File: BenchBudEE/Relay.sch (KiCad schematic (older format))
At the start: 0 parts

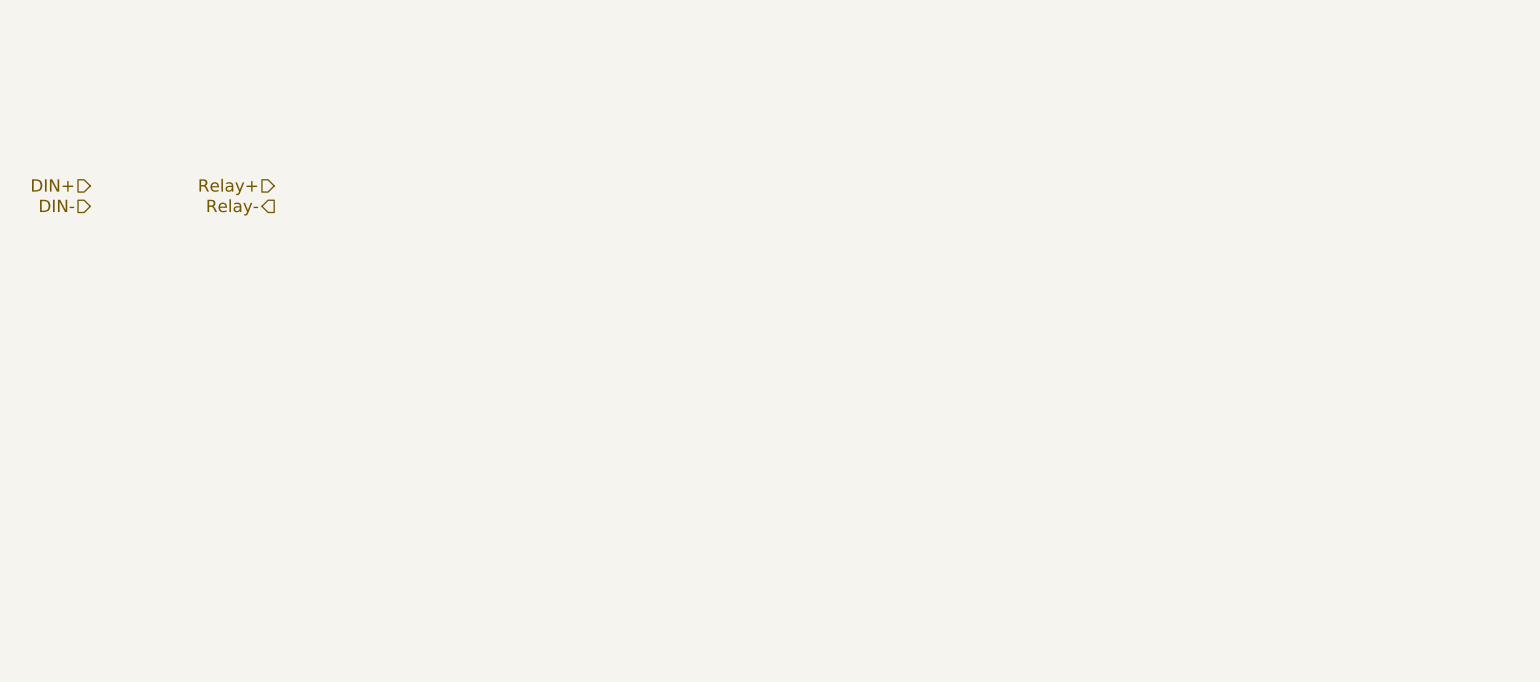
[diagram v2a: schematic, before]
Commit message: Implementing Relay schematic.
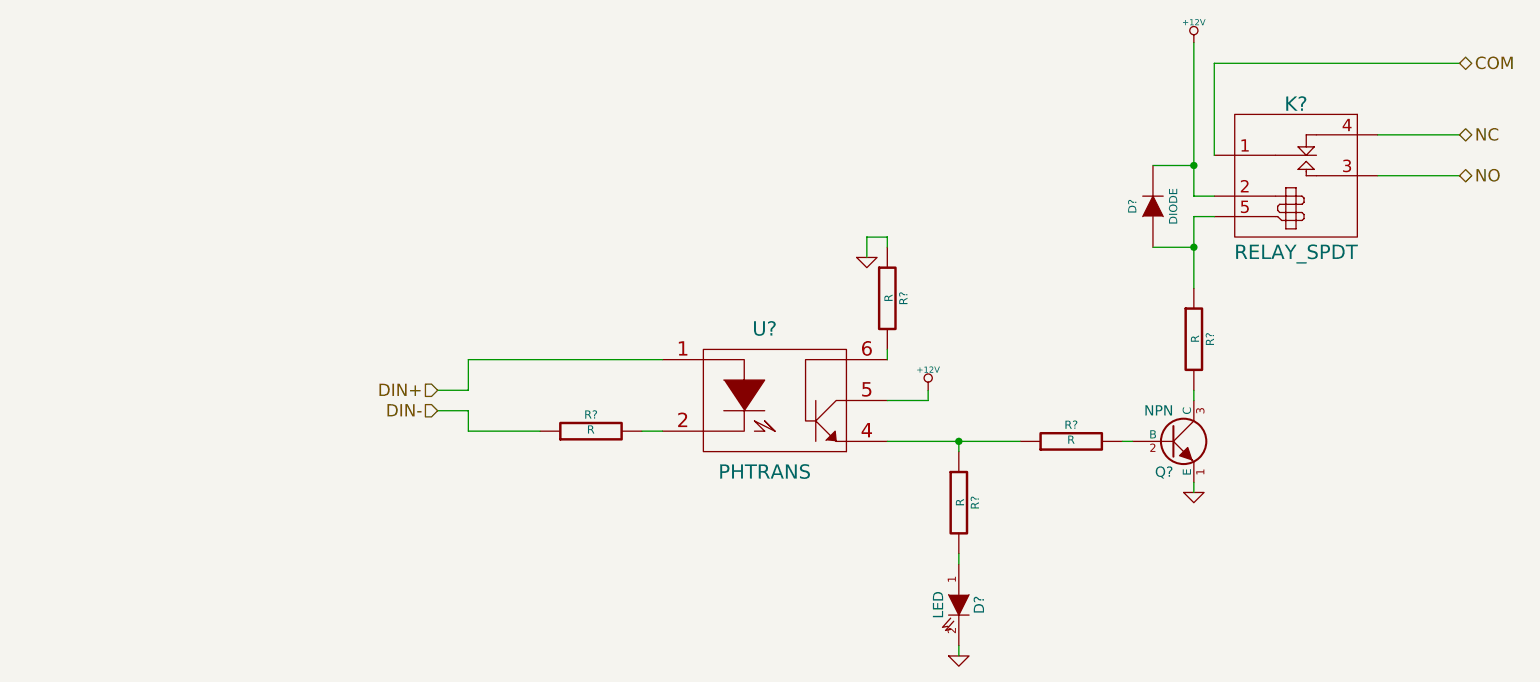
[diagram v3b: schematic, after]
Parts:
- added D?: LED, ~, symbol LED
- added D?: DIODE, ~, symbol DIODE
- added K?: RELAY_SPDT, ~, symbol RELAY_SPDT
- added Q?: NPN, ~, symbol NPN
- added R? (x5): R, ~, symbol R
- added U?: PHTRANS, ~, symbol PHTRANS
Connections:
- net DIN+: now also U?.1
- net DIN-: now also R?.1
- new net: D?.1 (A), K?.5 (COIL-), R?.1
- new net: Q?.2 (B), R?.2
- new net: Q?.3 (C), R?.2
- new net: R?.1, R?.1, U?.4
- new net: R?.2, U?.2
- new net: R?.2, U?.6
- new net: D?.1 (A), R?.2
- new net +12V: D?.2 (K), K?.2 (COIL+), U?.5
- new net COM: K?.1 (COM)
- new net GND: D?.2 (K), Q?.1 (E), R?.1
- new net NC: K?.4 (NC)
- new net NO: K?.3 (NO)
